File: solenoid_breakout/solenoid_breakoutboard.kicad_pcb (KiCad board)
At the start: 2 copper layers, 27 parts, among them J1 Conn_01x04_Pin, J2 Conn_01x04_Pin, J3 Conn_01x04_Pin, J4 Conn_01x04_Pin, J7 Conn_01x05, J8 Conn_01x05, Q2 AO3400A, Q5 AO3400A, Q6 AO3400A, Q7 AO3400A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

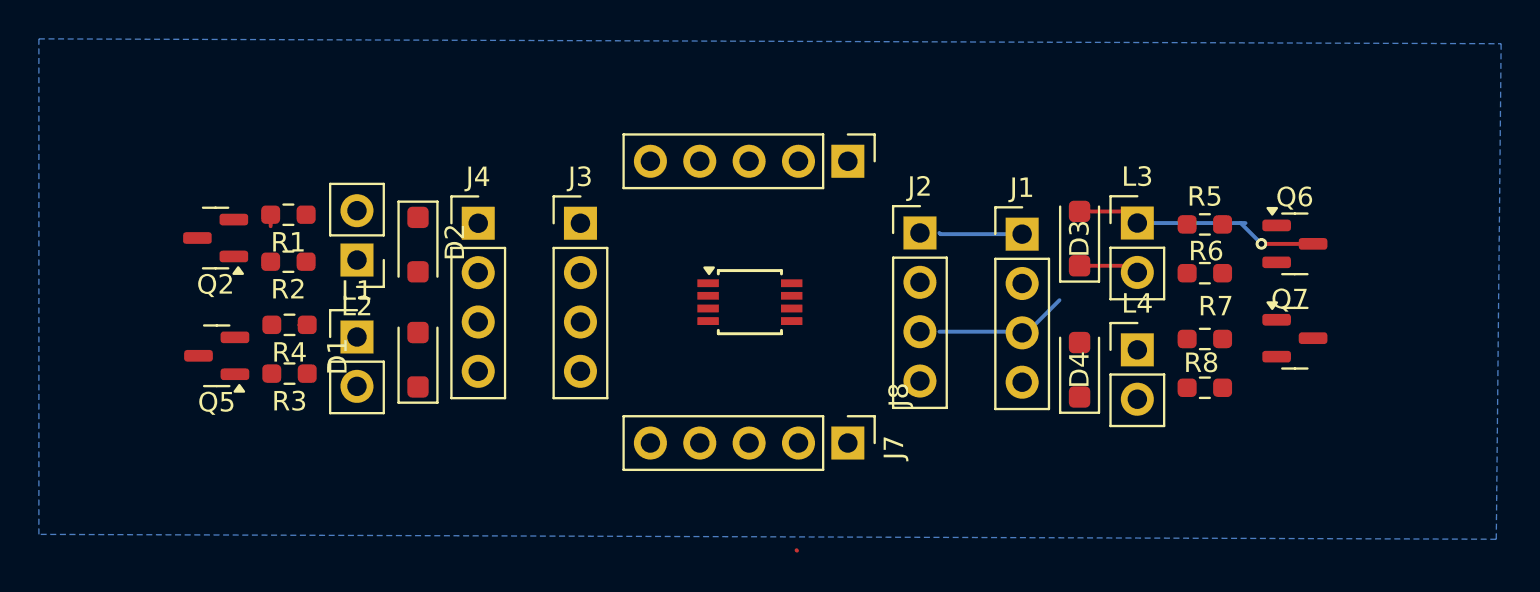
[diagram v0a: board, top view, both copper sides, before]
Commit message: solenoid breakout design finished awaiting review
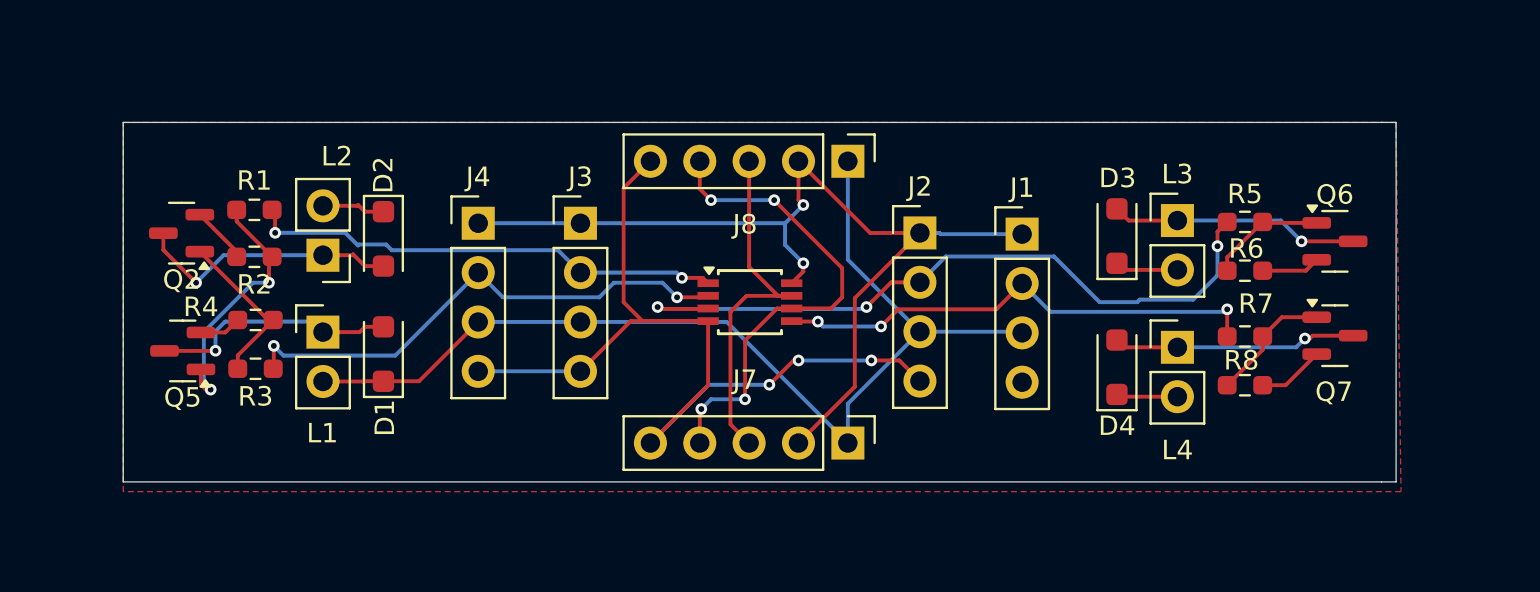
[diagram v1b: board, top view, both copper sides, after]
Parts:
- moved L3 2.07 mm to (112.2, 54.8)
- moved Q6 2.07 mm to (120.4, 55.9)
- moved R5 2.07 mm to (115.7, 54.9)
- moved R7 2.07 mm to (115.7, 60.8)
- moved R8 2.07 mm to (115.7, 63.3)
- moved L4 2.07 mm to (112.2, 61.3)
- moved Q7 2.07 mm to (120.4, 60.7)
- moved R6 2.07 mm to (115.7, 57.4)
- moved D3 1.93 mm to (109.1, 55.6)
- moved D4 1.93 mm to (109.1, 62.4)
- moved D2 1.80 mm to (71.4, 55.7)
- moved D1 1.80 mm to (71.4, 61.7)
- moved L1 1.77 mm to (68.3, 60.5)
- moved L2 1.77 mm to (68.3, 56.6)
- moved Q2 1.77 mm to (61.0, 55.5)
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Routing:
- net GND: track 1.03 -> 61.6 mm, vias 0 -> 3
- net +5V: track 6.99 -> 54.1 mm
- net +3.3V: track 4.52 -> 49.9 mm, vias 0 -> 2
- net Net-(J2-Pin_2): track 0.12 -> 37.3 mm, vias 0 -> 3
- net Net-(J4-Pin_2): track 0.11 -> 26.7 mm, vias 0 -> 2
- net Net-(J1-Pin_2): track 0.04 -> 25.5 mm, vias 0 -> 3
- net scl: track 0.00 -> 25.1 mm, vias 0 -> 4
- net Net-(J3-Pin_2): track 0.07 -> 24.8 mm, vias 0 -> 2
- net sda: track 0.00 -> 18.9 mm
- net Net-(D2-A): track 0.00 -> 13.7 mm, vias 0 -> 1
- net Net-(D4-A): track 0.00 -> 13.1 mm, vias 0 -> 1
- net Net-(Q5-G): track 0.17 -> 13.2 mm, vias 0 -> 2
- net Net-(D1-A): track 0.00 -> 12.8 mm, vias 0 -> 1
- net Net-(Q2-G): track 0.41 -> 8.91 mm
- net Net-(Q7-G): track 0.00 -> 6.46 mm
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- added copper zone on F.Cu, net GND
- removed copper zone on B.Cu, net (none)
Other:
- board outline added: 65.5 x 18.5 mm
- board text added: "Designed by Lakshay Yadav"
- board text added: "Property of Ghost Robotics"
- board text added: "et. al."

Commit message: revised solenoid board
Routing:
- net GND: track 61.6 -> 97.4 mm, vias 3 -> 7
- net Net-(J2-Pin_2): track 37.3 -> 37.9 mm, vias 3 -> 4
- net +5V: track 54.1 -> 54.6 mm, vias 0 -> 1
- net Net-(J3-Pin_2): vias 2 -> 3
- net Net-(J4-Pin_2): vias 2 -> 3
- net Net-(J1-Pin_2): vias 3 -> 4
- net (no net): vias 0 -> 30
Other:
- outline, holes or cut-outs redrawn
